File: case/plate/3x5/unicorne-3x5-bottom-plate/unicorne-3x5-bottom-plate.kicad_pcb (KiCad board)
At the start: 2 copper layers, 114.8 x 91.4 mm, 6 parts, among them J3 Tenting Puck

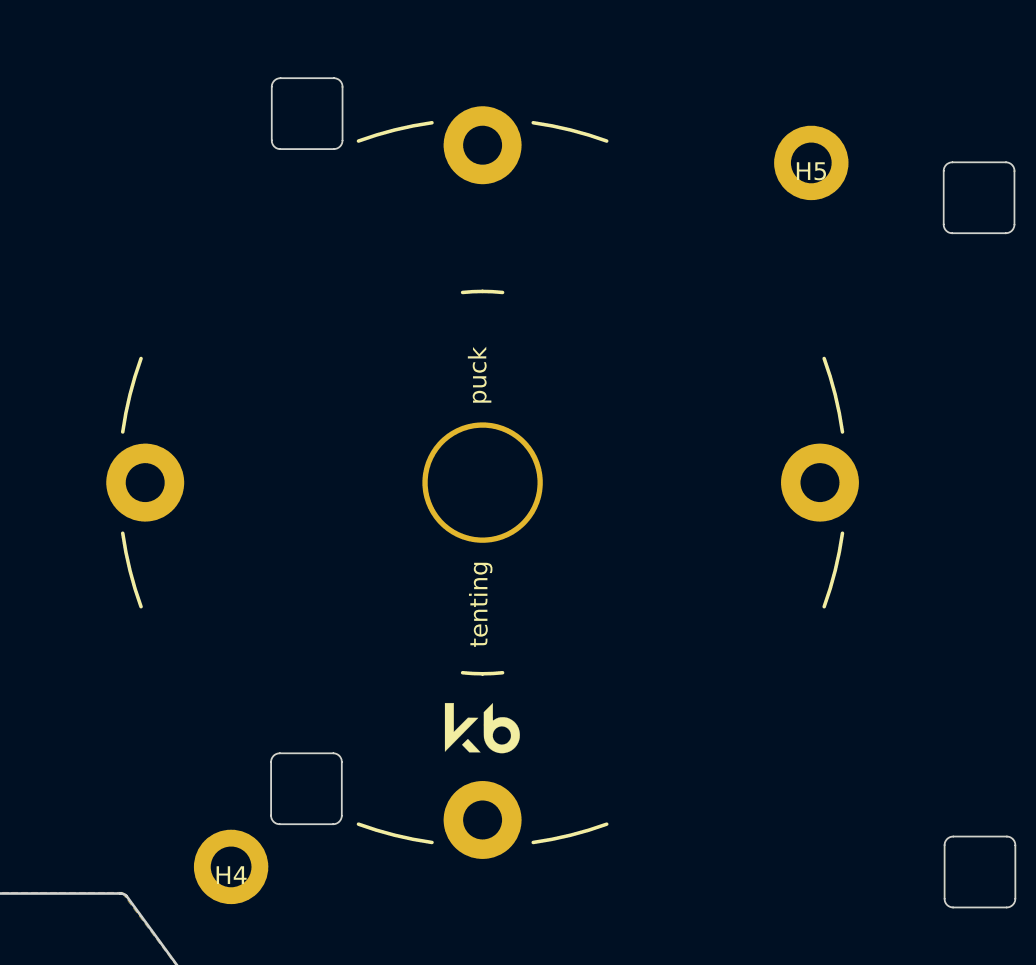
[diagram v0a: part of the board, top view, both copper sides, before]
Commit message: Docs (#5)
* added build guide

* correct link
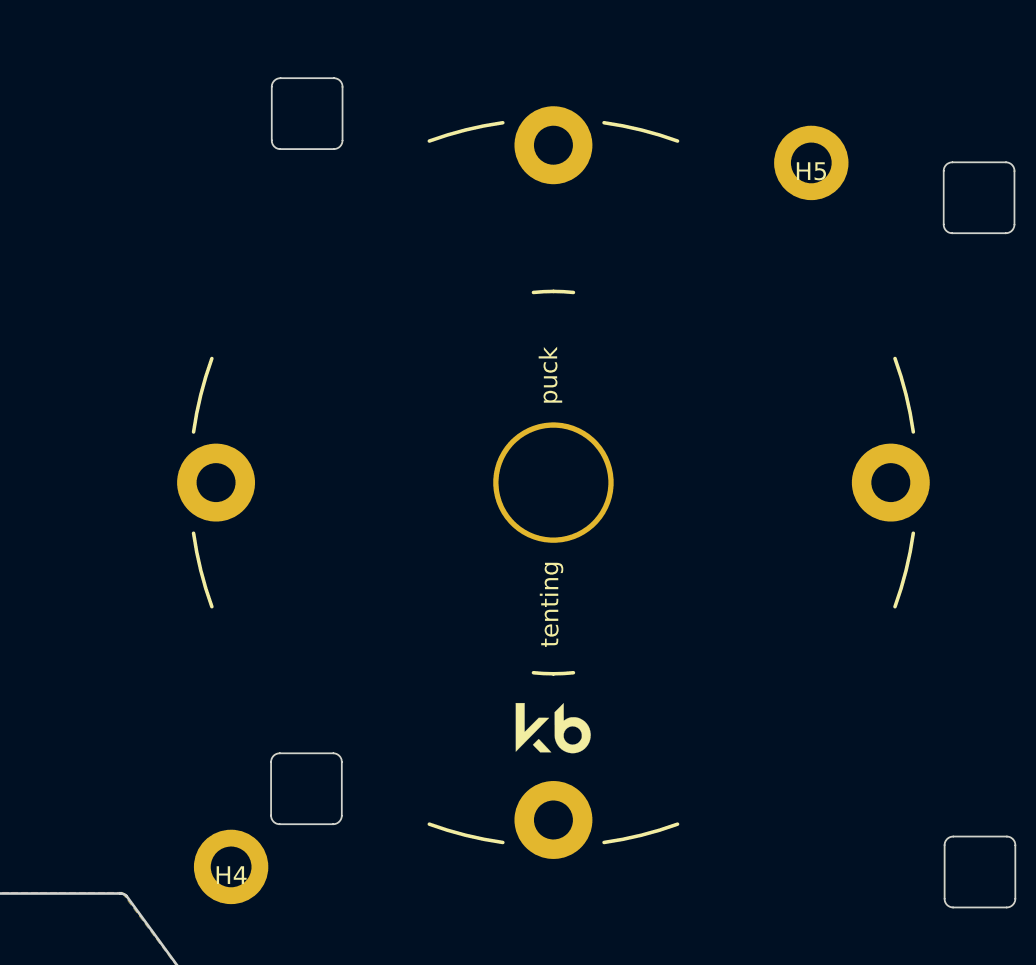
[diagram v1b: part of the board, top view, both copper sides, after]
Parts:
- moved J3 4.00 mm to (140.8, 101.1)
